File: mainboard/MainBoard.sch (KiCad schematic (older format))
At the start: 34 parts, among them J1 CONN_1x4, J2 CONN_2X3, J3 CONN_2X3, J5 SWDEBUG_CONNECTOR, J7 CONN_2X12, J8 CONN_1X2, U1 VX07805-1000, U2 TPS2115A, U3 ld1117s33

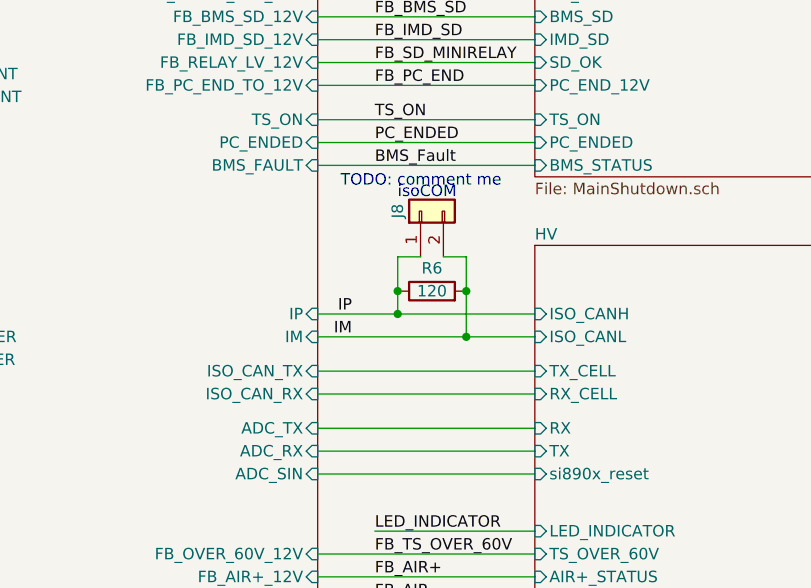
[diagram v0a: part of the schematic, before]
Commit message: Added 64pin mcu and moved isocanspi to HV sheet
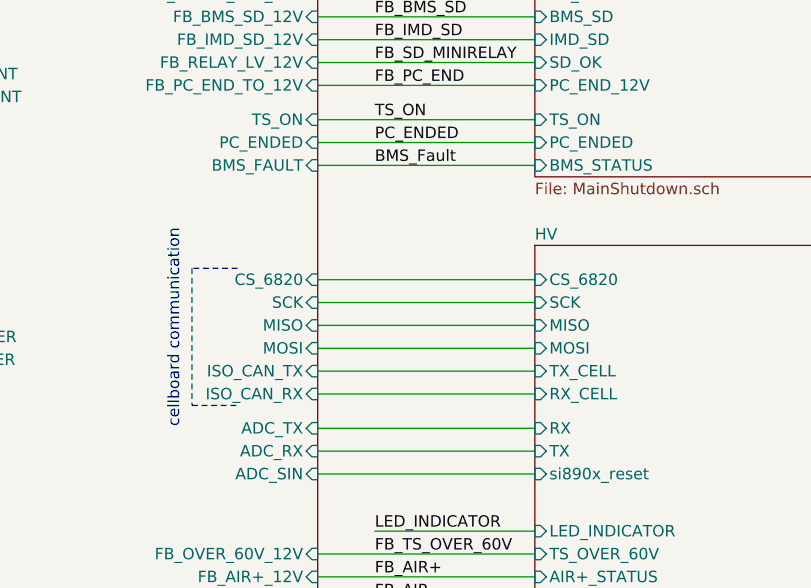
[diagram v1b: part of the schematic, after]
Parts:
- removed J8: CONN_1X2, MainBoard:Molex_Micro-Fit_3.0_43650-0215_1x02_P3.00mm_Vertical, symbol Connector_Generic:Conn_01x02
- removed R6: 120, Resistor_SMD:R_0805_2012Metric, symbol Device:R
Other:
- note added: "cellboard communication"
- note removed: "isoCOM"
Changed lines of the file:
@@
 Sheet 1 4
 Title ""
-Date ""
-Rev ""
+Date "2020-12-10"
+Rev "v1.1_wip"
 Comp ""
 Comment1 ""
@@
 	0    -1   -1   0
 $EndComp
-Text Label 3300 6050 2    50   ~ 0
-IM
-Text Label 3300 5950 2    50   ~ 0
-IP
 Connection ~ 7700 1050
 Wire Wire Line
@@
 F8 "RX_CELL" I L 4100 6300 50
 F9 "TX_CELL" I L 4100 6200 50
-F10 "ISO_CANH" I L 4100 5950 50
-F11 "ISO_CANL" I L 4100 6050 50
-F12 "si890x_reset" I L 4100 6650 50
-F13 "AIR-_STATUS" I L 4100 7200 50
-F14 "AIR+_STATUS" I L 4100 7100 50
-F15 "TS_OVER_60V" I L 4100 7000 50
+F10 "si890x_reset" I L 4100 6650 50
+F11 "AIR-_STATUS" I L 4100 7200 50
+F12 "AIR+_STATUS" I L 4100 7100 50
+F13 "TS_OVER_60V" I L 4100 7000 50
+F14 "CS_6820" I L 4100 5800 50
+F15 "SCK" I L 4100 5900 50
+F16 "MISO" I L 4100 6000 50
+F17 "MOSI" I L 4100 6100 50
 $EndSheet
 $Comp
@@
 F23 "BSPD_SIG" I L 4100 4050 50
 $EndSheet
-$Sheet
-S 1250 3350 1900 3900
-U 5DF398FB
-F0 "AMS" 50
-F1 "MCU.sch" 50
-F2 "FROM_SD" I R 3150 3550 50
-F3 "TO_TSMS" I R 3150 3650 50
-F4 "FROM_TSMS" I R 3150 3750 50
-F5 "IP" I R 3150 5950 50
-F6 "IM" I R 3150 6050 50
-F7 "HIGH_CURRENT" I L 1250 5000 50
-F8 "LOW_CURRENT" I L 1250 4900 50
-F9 "CAN+" I L 1250 4500 50
-F10 "CHARGE" I L 1250 4750 50
-F11 "TX_DEBUGGER" I L 1250 6150 50
-F12 "RX_DEBUGGER" I L 1250 6050 50
-F13 "SWDIO" I L 1250 5850 50
-F14 "SWCLK" I L 1250 5950 50
-F15 "NRST" I L 1250 5750 50
-F16 "IMD_PWM" I L 1250 5150 50
-F17 "CAN-" I L 1250 4600 50
-F18 "ADC_TX" I R 3150 6450 50
-F19 "ADC_RX" I R 3150 6550 50
-F20 "ISO_CAN_TX" I R 3150 6200 50
-F21 "ISO_CAN_RX" I R 3150 6300 50
-F22 "SWO" I L 1250 5650 50
-F23 "ADC_SIN" I R 3150 6650 50
-F24 "PC_ENDED" I R 3150 5200 50
-F25 "TS_ON" I R 3150 5100 50
-F26 "BMS_FAULT" I R 3150 5300 50
-F27 "FB_IMD_FAULT_12V" I R 3150 4150 50
-F28 "FB_LATCH_BMS_12V" I R 3150 4450 50
-F29 "FB_LATCH_IMD_12V" I R 3150 4550 50
-F30 "FB_BMS_SD_12V" I R 3150 4650 50
-F31 "FB_IMD_SD_12V" I R 3150 4750 50
-F32 "FB_RELAY_LV_12V" I R 3150 4850 50
-F33 "FB_AIR-_12V" I R 3150 7200 50
-F34 "FB_AIR+_12V" I R 3150 7100 50
-F35 "FB_OVER_60V_12V" I R 3150 7000 50
-F36 "FB_TS_ON_TO_12V" I R 3150 4350 50
-F37 "FB_BMS_TO_12V" I R 3150 4250 50
-F38 "FB_PC_END_TO_12V" I R 3150 4950 50
-$EndSheet
 Text Label 3400 4250 0    50   ~ 0
 FB_BMS
@@
 	1    0    0    -1
 $EndComp
-Wire Wire Line
-	3800 6050 4100 6050
-Wire Wire Line
-	3150 6050 3800 6050
-Connection ~ 3800 6050
-Wire Wire Line
-	3500 5950 4100 5950
-Wire Wire Line
-	3150 5950 3500 5950
-Connection ~ 3500 5950
-Wire Wire Line
-	3600 5700 3500 5700
-Wire Wire Line
-	3700 5700 3800 5700
-$Comp
-L Device:R R6
-U 1 1 5F272E0B
-P 3650 5850
-AR Path="/5F272E0B" Ref="R6"  Part="1"
-AR Path="/5DF398FB/5F272E0B" Ref="R?"  Part="1"
-F 0 "R6" V 3750 5850 50  0000 C CNN
-F 1 "120" V 3650 5850 50  0000 C CNN
-F 2 "Resistor_SMD:R_0805_2012Metric" V 3580 5850 50  0001 C CNN
-F 3 "~" H 3650 5850 50  0001 C CNN
-	1    3650 5850
-	0    -1   -1   0
-$EndComp
-$Comp
-L Connector_Generic:Conn_01x02 J8
-U 1 1 5E165F43
-P 3600 5500
-AR Path="/5E165F43" Ref="J8"  Part="1"
-AR Path="/5DF398FB/5E165F43" Ref="J?"  Part="1"
-AR Path="/5DE633EC/5E165F43" Ref="J?"  Part="1"
-F 0 "J8" H 3600 5600 50  0000 C CNN
-F 1 "CONN_1X2" V 3700 5450 50  0001 C CNN
-F 2 "MainBoard:Molex_Micro-Fit_3.0_43650-0215_1x02_P3.00mm_Vertical" H 3600 5500 50  0001 C CNN
-F 3 "~" H 3600 5500 50  0001 C CNN
-	1    3600 5500
-	0    -1   -1   0
-$EndComp
 Text Notes 7050 6100 1    50   ~ 0
 DHAB S/160
@@
 Text Notes 4050 2950 1    50   ~ 0
 CONN_RECT
-Text Notes 3500 5450 0    50   ~ 0
-isoCOM
 Wire Wire Line
 	4100 4050 3700 4050
@@
 $EndComp
 Wire Wire Line
-	3800 5700 3800 5850
-Wire Wire Line
-	3500 5700 3500 5850
-Wire Wire Line
 	8000 2100 8300 2100
 Text Label 8000 2100 0    50   ~ 0
@@
 Wire Wire Line
 	8300 2100 8700 2100
-Connection ~ 3800 5850
-Wire Wire Line
-	3800 5850 3800 6050
-Connection ~ 3500 5850
-Wire Wire Line
-	3500 5850 3500 5950
 Text Notes 8050 1800 0    50   ~ 0
 Switch for when USB is inserted
@@
 Wire Notes Line
 	500  3450 4050 3450
-Text Notes 3250 5400 0    50   ~ 0
-TODO: comment me
 Wire Notes Line
 	11150 4250 10100 4250
@@
 Wire Notes Line
 	7450 2950 7450 600
+Wire Wire Line
+	3150 5800 4100 5800
+Wire Wire Line
+	3150 5900 4100 5900
+Wire Wire Line
+	3150 6000 4100 6000
+Wire Wire Line
+	4100 6100 3150 6100
+Wire Notes Line
+	2800 5750 2600 5750
+Wire Notes Line
+	2600 5750 2600 6350
+Wire Notes Line
+	2600 6350 2800 6350
+Text Notes 2550 6450 1    50   ~ 0
+cellboard communication
+$Sheet
+S 1250 3350 1900 3900
+U 5DF398FB
+F0 "AMS" 50
+F1 "MCU.sch" 50
+F2 "FROM_SD" I R 3150 3550 50
+F3 "TO_TSMS" I R 3150 3650 50
+F4 "FROM_TSMS" I R 3150 3750 50
+F5 "HIGH_CURRENT" I L 1250 5000 50
+F6 "LOW_CURRENT" I L 1250 4900 50
+F7 "CAN+" I L 1250 4500 50
+F8 "CHARGE" I L 1250 4750 50
+F9 "TX_DEBUGGER" I L 1250 6150 50
+F10 "RX_DEBUGGER" I L 1250 6050 50
+F11 "SWDIO" I L 1250 5850 50
+F12 "SWCLK" I L 1250 5950 50
+F13 "NRST" I L 1250 5750 50
+F14 "IMD_PWM" I L 1250 5150 50
+F15 "CAN-" I L 1250 4600 50
+F16 "ADC_TX" I R 3150 6450 50
+F17 "ADC_RX" I R 3150 6550 50
+F18 "ISO_CAN_TX" I R 3150 6200 50
+F19 "ISO_CAN_RX" I R 3150 6300 50
+F20 "SWO" I L 1250 5650 50
+F21 "ADC_SIN" I R 3150 6650 50
+F22 "PC_ENDED" I R 3150 5200 50
+F23 "TS_ON" I R 3150 5100 50
+F24 "BMS_FAULT" I R 3150 5300 50
+F25 "FB_IMD_FAULT_12V" I R 3150 4150 50
+F26 "FB_LATCH_BMS_12V" I R 3150 4450 50
+F27 "FB_LATCH_IMD_12V" I R 3150 4550 50
+F28 "FB_BMS_SD_12V" I R 3150 4650 50
+F29 "FB_IMD_SD_12V" I R 3150 4750 50
+F30 "FB_RELAY_LV_12V" I R 3150 4850 50
+F31 "FB_AIR-_12V" I R 3150 7200 50
+F32 "FB_AIR+_12V" I R 3150 7100 50
+F33 "FB_OVER_60V_12V" I R 3150 7000 50
+F34 "FB_TS_ON_TO_12V" I R 3150 4350 50
+F35 "FB_BMS_TO_12V" I R 3150 4250 50
+F36 "FB_PC_END_TO_12V" I R 3150 4950 50
+F37 "CS_6820" I R 3150 5800 50
+F38 "SCK" I R 3150 5900 50
+F39 "MISO" I R 3150 6000 50
+F40 "MOSI" I R 3150 6100 50
+$EndSheet
 $EndSCHEMATC

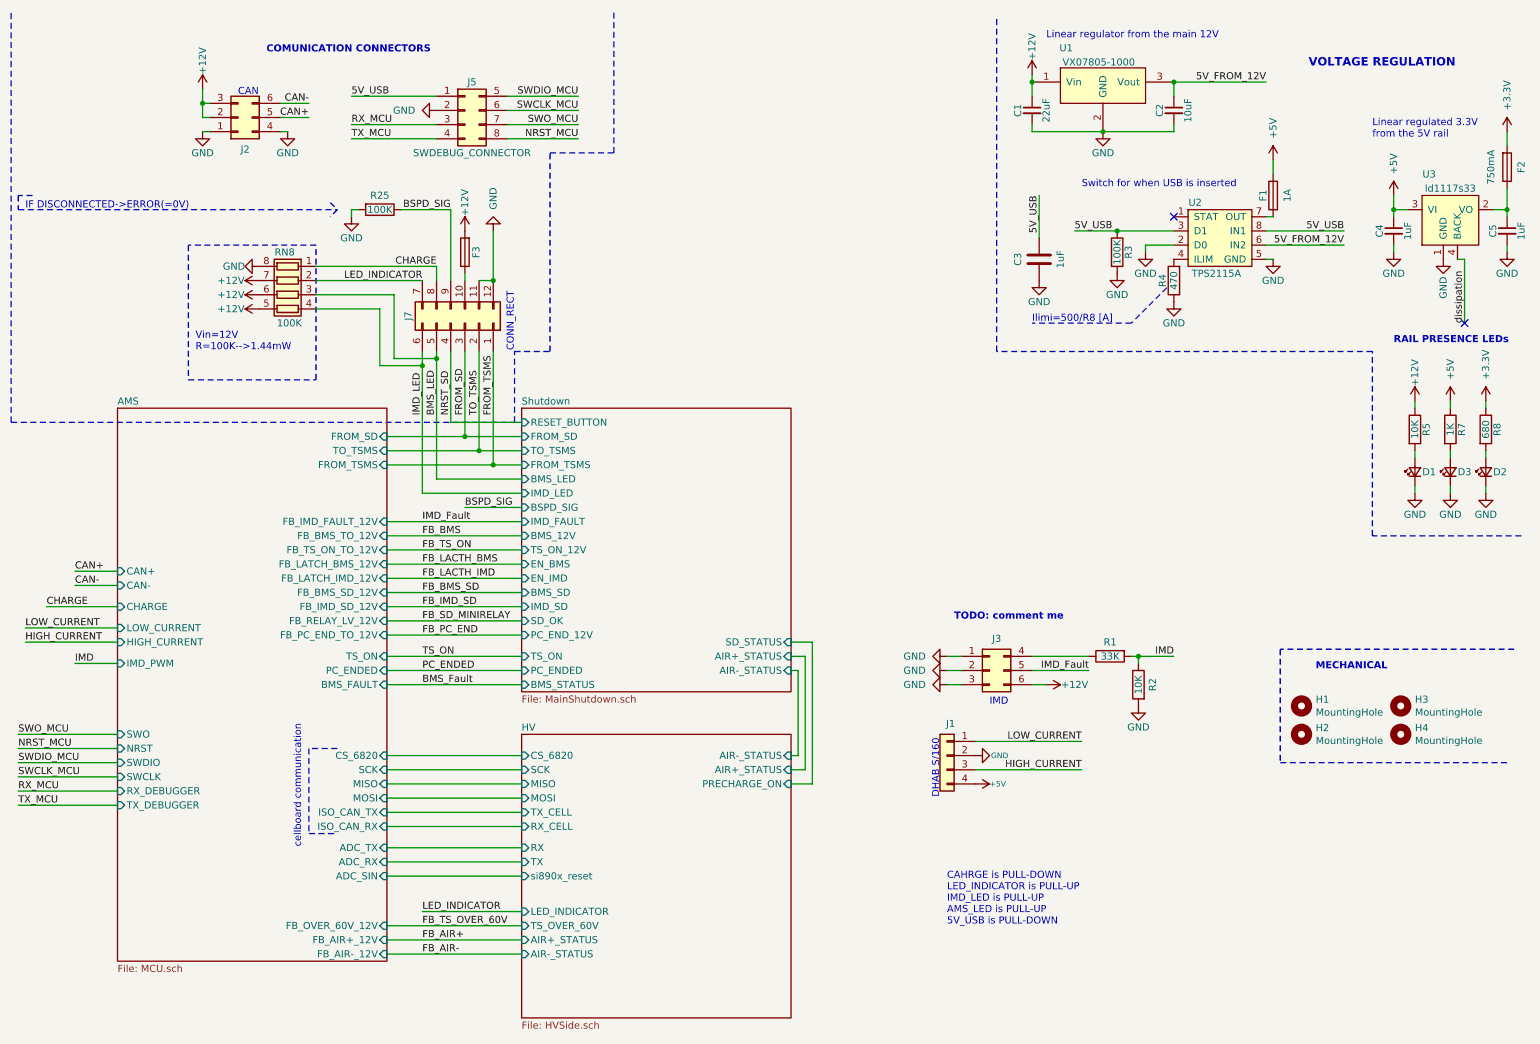
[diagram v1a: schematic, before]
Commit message: 64pin, testpoints, commenting, general refactoring
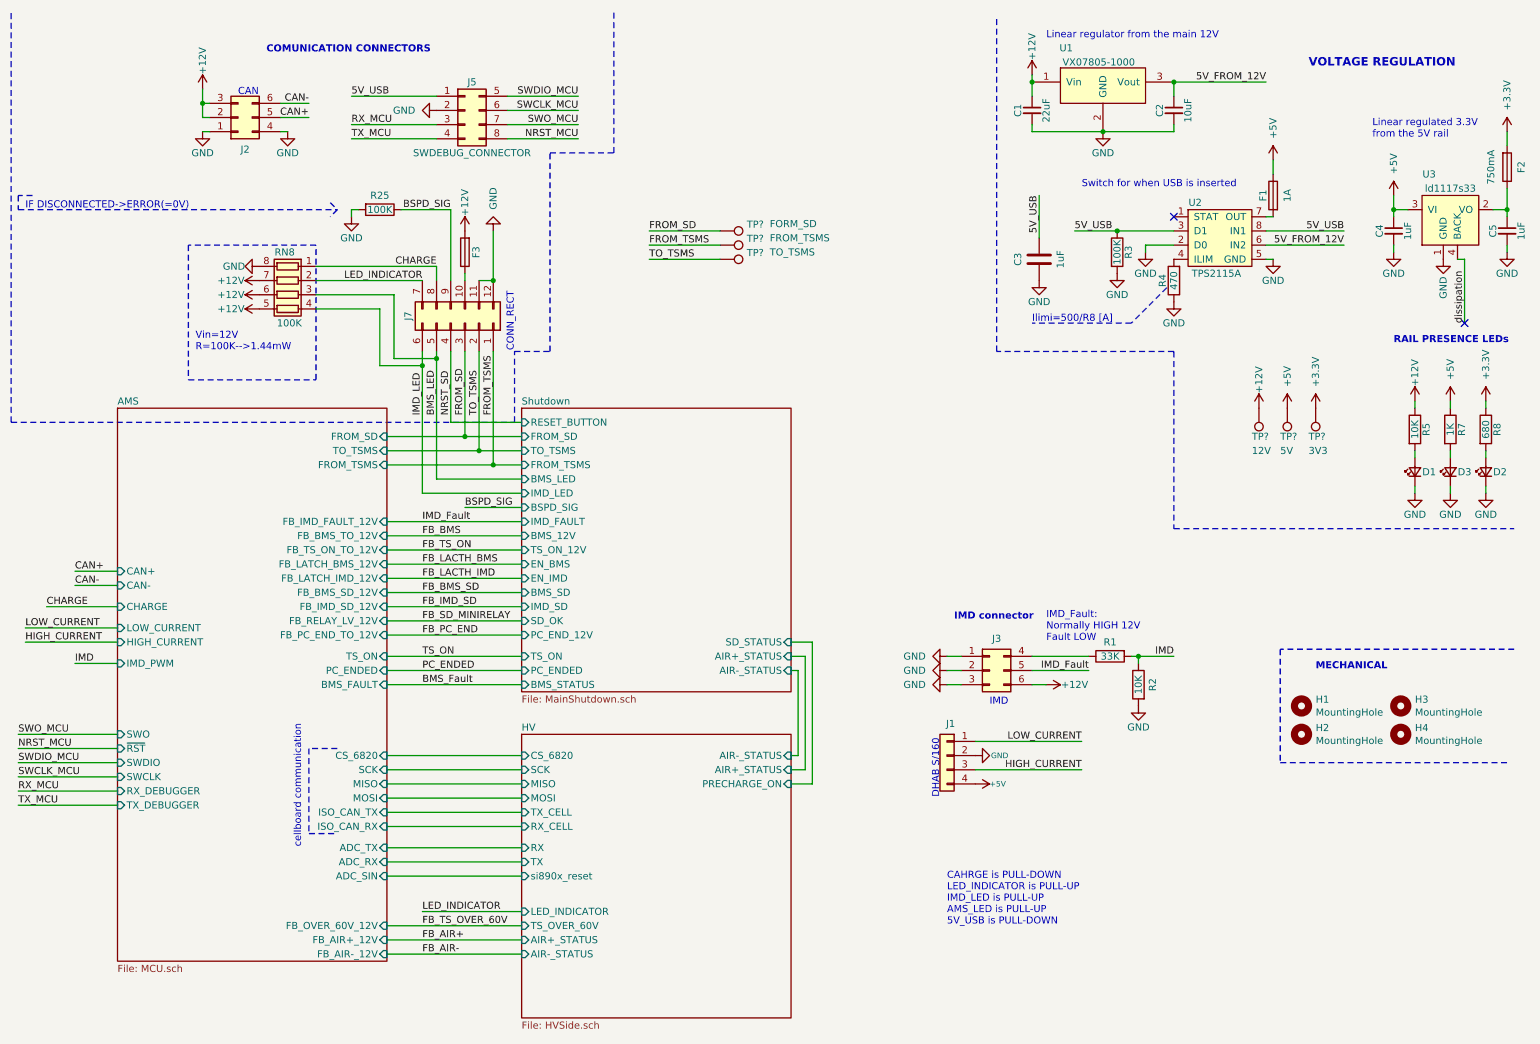
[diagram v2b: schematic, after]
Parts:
- added TP?: FORM_SD, symbol Connector:TestPoint
- added TP?: FROM_TSMS, symbol Connector:TestPoint
- added TP?: TO_TSMS, symbol Connector:TestPoint
- added TP?: 3V3, symbol Connector:TestPoint
- added TP?: 5V, symbol Connector:TestPoint
- added TP?: 12V, symbol Connector:TestPoint
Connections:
- net +12V: now also TP?.1
- net +3V3: now also TP?.1
- net +5V: now also TP?.1
- net FROM_SD: now also TP?.1
- net FROM_TSMS: now also TP?.1
- net TO_TSMS: now also TP?.1
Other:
- note added: "IMD connector"
- note added: "IMD_Fault:\nNormally HIGH 12V\nFault LOW"
- note removed: "TODO: comment me"
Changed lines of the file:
@@
 Linear regulated 3.3V \nfrom the 5V rail
 Text Notes 7150 4850 0    50   ~ 10
-TODO: comment me
+IMD connector
 Text Notes 2300 850  0    50   ~ 10
 COMUNICATION CONNECTORS
@@
 	500  3450 4050 3450
 Wire Notes Line
-	11150 4250 10100 4250
-Wire Notes Line
-	10100 4250 10100 2950
-Wire Notes Line
-	10100 2950 7450 2950
+	8700 2950 7450 2950
 Wire Notes Line
 	7450 2950 7450 600
@@
 F11 "SWDIO" I L 1250 5850 50
 F12 "SWCLK" I L 1250 5950 50
-F13 "NRST" I L 1250 5750 50
+F13 "~RST~" I L 1250 5750 50
 F14 "IMD_PWM" I L 1250 5150 50
 F15 "CAN-" I L 1250 4600 50
@@
 F40 "MOSI" I R 3150 6100 50
 $EndSheet
+Text Notes 7800 5000 0    50   ~ 0
+IMD_Fault:\nNormally HIGH 12V\nFault LOW
+Text Label 5000 2100 0    50   ~ 0
+FROM_SD
+Text Label 5000 2200 0    50   ~ 0
+FROM_TSMS
+Text Label 5000 2300 0    50   ~ 0
+TO_TSMS
+$Comp
+L Connector:TestPoint TP?
+U 1 1 605C7740
+P 5500 2100
+F 0 "TP?" V 5454 2288 50  0000 L CNN
+F 1 "FORM_SD" V 5450 2450 50  0000 L CNN
+F 2 "" H 5700 2100 50  0001 C CNN
+F 3 "~" H 5700 2100 50  0001 C CNN
+	1    5500 2100
+	0    1    1    0
+$EndComp
+$Comp
+L Connector:TestPoint TP?
+U 1 1 605C7DFE
+P 5500 2200
+F 0 "TP?" V 5454 2388 50  0000 L CNN
+F 1 "FROM_TSMS" V 5450 2550 50  0000 L CNN
+F 2 "" H 5700 2200 50  0001 C CNN
+F 3 "~" H 5700 2200 50  0001 C CNN
+	1    5500 2200
+	0    1    1    0
+$EndComp
+$Comp
+L Connector:TestPoint TP?
+U 1 1 605C7FA8
+P 5500 2300
+F 0 "TP?" V 5454 2488 50  0000 L CNN
+F 1 "TO_TSMS" V 5450 2650 50  0000 L CNN
+F 2 "" H 5700 2300 50  0001 C CNN
+F 3 "~" H 5700 2300 50  0001 C CNN
+	1    5500 2300
+	0    1    1    0
+$EndComp
+Wire Wire Line
+	5000 2100 5500 2100
+Wire Wire Line
+	5500 2200 5000 2200
+Wire Wire Line
+	5000 2300 5500 2300
+$Comp
+L Connector:TestPoint TP?
+U 1 1 6060C55B
+P 9700 3350
+F 0 "TP?" H 9750 3550 50  0000 R CNN
+F 1 "3V3" H 9750 3650 50  0000 R CNN
+F 2 "" H 9900 3350 50  0001 C CNN
+F 3 "~" H 9900 3350 50  0001 C CNN
+	1    9700 3350
+	-1   0    0    1
+$EndComp
+$Comp
+L Connector:TestPoint TP?
+U 1 1 6060CEE1
+P 9500 3350
+F 0 "TP?" H 9550 3550 50  0000 R CNN
+F 1 "5V" H 9550 3650 50  0000 R CNN
+F 2 "" H 9700 3350 50  0001 C CNN
+F 3 "~" H 9700 3350 50  0001 C CNN
+	1    9500 3350
+	-1   0    0    1
+$EndComp
+$Comp
+L Connector:TestPoint TP?
+U 1 1 6060D124
+P 9300 3350
+F 0 "TP?" H 9350 3550 50  0000 R CNN
+F 1 "12V" H 9350 3650 50  0000 R CNN
+F 2 "" H 9500 3350 50  0001 C CNN
+F 3 "~" H 9500 3350 50  0001 C CNN
+	1    9300 3350
+	-1   0    0    1
+$EndComp
+$Comp
+L power:+12V #PWR?
+U 1 1 6061F869
+P 9300 3350
+AR Path="/6061F869" Ref="#PWR?"  Part="1"
+AR Path="/5DE633EC/6061F869" Ref="#PWR?"  Part="1"
+F 0 "#PWR?" H 9300 3200 50  0001 C CNN
+F 1 "+12V" V 9300 3550 50  0000 C CNN
+F 2 "" H 9300 3350 50  0001 C CNN
+F 3 "" H 9300 3350 50  0001 C CNN
+	1    9300 3350
+	1    0    0    -1
+$EndComp
+$Comp
+L power:+5V #PWR?
+U 1 1 6061F86F
+P 9500 3350
+AR Path="/6061F86F" Ref="#PWR?"  Part="1"
+AR Path="/5DE633EC/6061F86F" Ref="#PWR?"  Part="1"
+F 0 "#PWR?" H 9500 3200 50  0001 C CNN
+F 1 "+5V" V 9500 3500 50  0000 L CNN
+F 2 "" H 9500 3350 50  0001 C CNN
+F 3 "" H 9500 3350 50  0001 C CNN
+	1    9500 3350
+	1    0    0    -1
+$EndComp
+$Comp
+L power:+3.3V #PWR?
+U 1 1 6061F875
+P 9700 3350
+AR Path="/6061F875" Ref="#PWR?"  Part="1"
+AR Path="/5DE633EC/6061F875" Ref="#PWR?"  Part="1"
+F 0 "#PWR?" H 9700 3200 50  0001 C CNN
+F 1 "+3.3V" V 9700 3500 50  0000 L CNN
+F 2 "" H 9700 3350 50  0001 C CNN
+F 3 "" H 9700 3350 50  0001 C CNN
+	1    9700 3350
+	1    0    0    -1
+$EndComp
+Wire Notes Line
+	8700 4200 11100 4200
+Wire Notes Line
+	8700 2950 8700 4200
 $EndSCHEMATC
